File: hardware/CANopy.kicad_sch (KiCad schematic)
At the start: 11 parts, among them J1 RPi_GPIO, J2 CAN0, J3 CAN1, J4 CAN2, U7 AT24C32

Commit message: feat: rename to CANopy
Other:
- sheet CAN0: file can_channel.kicad_sch -> CANopy_branch.kicad_sch
- sheet CAN1: file can_channel.kicad_sch -> CANopy_branch.kicad_sch
- sheet CAN2: file can_channel.kicad_sch -> CANopy_branch.kicad_sch
- title: CAN Hat -> CANopy
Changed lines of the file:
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@@
 	(paper "User" 203.2 127)
 	(title_block
-		(title "CAN Hat")
+		(title "CANopy")
 		(date "2026-04-25")
 		(rev "1")
@@
 		)
 		(instances
-			(project "can-hat"
+			(project "CANopy"
 				(path "/bfdea6a0-b5c8-4489-9fa0-a972c3ff35f2"
 					(reference "J4")
@@
 		)
 		(instances
-			(project "can-hat"
+			(project "CANopy"
 				(path "/bfdea6a0-b5c8-4489-9fa0-a972c3ff35f2"
 					(reference "#PWR040")
@@
 		)
 		(instances
-			(project "can-hat"
+			(project "CANopy"
 				(path "/bfdea6a0-b5c8-4489-9fa0-a972c3ff35f2"
 					(reference "#PWR054")
@@
 		)
 		(instances
-			(project "can-hat"
+			(project "CANopy"
 				(path "/bfdea6a0-b5c8-4489-9fa0-a972c3ff35f2"
 					(reference "C14")
@@
 		)
 		(instances
-			(project "can-hat"
+			(project "CANopy"
 				(path "/bfdea6a0-b5c8-4489-9fa0-a972c3ff35f2"
 					(reference "#PWR041")
@@
 		)
 		(instances
-			(project "can-hat"
+			(project "CANopy"
 				(path "/bfdea6a0-b5c8-4489-9fa0-a972c3ff35f2"
 					(reference "R9")
@@
 		)
 		(instances
-			(project "can-hat"
+			(project "CANopy"
 				(path "/bfdea6a0-b5c8-4489-9fa0-a972c3ff35f2"
 					(reference "#PWR028")
@@
 		)
 		(instances
-			(project "can-hat"
+			(project "CANopy"
 				(path "/bfdea6a0-b5c8-4489-9fa0-a972c3ff35f2"
 					(reference "#PWR030")
@@
 		)
 		(instances
-			(project "can-hat"
+			(project "CANopy"
 				(path "/bfdea6a0-b5c8-4489-9fa0-a972c3ff35f2"
 					(reference "#PWR043")
@@
 		)
 		(instances
-			(project "can-hat"
+			(project "CANopy"
 				(path "/bfdea6a0-b5c8-4489-9fa0-a972c3ff35f2"
 					(reference "#PWR042")
@@
 		)
 		(instances
-			(project "can-hat"
+			(project "CANopy"
 				(path "/bfdea6a0-b5c8-4489-9fa0-a972c3ff35f2"
 					(reference "#PWR052")
@@
 		)
 		(instances
-			(project "can-hat"
+			(project "CANopy"
 				(path "/bfdea6a0-b5c8-4489-9fa0-a972c3ff35f2"
 					(reference "#PWR018")
@@
 		)
 		(instances
-			(project "can-hat"
+			(project "CANopy"
 				(path "/bfdea6a0-b5c8-4489-9fa0-a972c3ff35f2"
 					(reference "#PWR046")
@@
 		)
 		(instances
-			(project "can-hat"
+			(project "CANopy"
 				(path "/bfdea6a0-b5c8-4489-9fa0-a972c3ff35f2"
 					(reference "R8")
@@
 		)
 		(instances
-			(project "can-hat"
+			(project "CANopy"
 				(path "/bfdea6a0-b5c8-4489-9fa0-a972c3ff35f2"
 					(reference "#PWR047")
@@
 		)
 		(instances
-			(project "can-hat"
+			(project "CANopy"
 				(path "/bfdea6a0-b5c8-4489-9fa0-a972c3ff35f2"
 					(reference "#PWR049")
@@
 		)
 		(instances
-			(project "can-hat"
+			(project "CANopy"
 				(path "/bfdea6a0-b5c8-4489-9fa0-a972c3ff35f2"
 					(reference "#PWR050")
@@
 		)
 		(instances
-			(project "can-hat"
+			(project "CANopy"
 				(path "/bfdea6a0-b5c8-4489-9fa0-a972c3ff35f2"
 					(reference "#FLG02")
@@
 		)
 		(instances
-			(project "can-hat"
+			(project "CANopy"
 				(path "/bfdea6a0-b5c8-4489-9fa0-a972c3ff35f2"
 					(reference "J3")
@@
 		)
 		(instances
-			(project "can-hat"
+			(project "CANopy"
 				(path "/bfdea6a0-b5c8-4489-9fa0-a972c3ff35f2"
 					(reference "#PWR045")
@@
 		)
 		(instances
-			(project "can-hat"
+			(project "CANopy"
 				(path "/bfdea6a0-b5c8-4489-9fa0-a972c3ff35f2"
 					(reference "#PWR053")
@@
 		)
 		(instances
-			(project "can-hat"
+			(project "CANopy"
 				(path "/bfdea6a0-b5c8-4489-9fa0-a972c3ff35f2"
 					(reference "#PWR051")
@@
 		)
 		(instances
-			(project "can-hat"
+			(project "CANopy"
 				(path "/bfdea6a0-b5c8-4489-9fa0-a972c3ff35f2"
 					(reference "#FLG03")
@@
 		)
 		(instances
-			(project "can-hat"
+			(project "CANopy"
 				(path "/bfdea6a0-b5c8-4489-9fa0-a972c3ff35f2"
 					(reference "#PWR055")
@@
 		)
 		(instances
-			(project "can-hat"
+			(project "CANopy"
 				(path "/bfdea6a0-b5c8-4489-9fa0-a972c3ff35f2"
 					(reference "#PWR048")
@@
 		)
 		(instances
-			(project "can-hat"
+			(project "CANopy"
 				(path "/bfdea6a0-b5c8-4489-9fa0-a972c3ff35f2"
 					(reference "#PWR016")
@@
 		)
 		(instances
-			(project "can-hat"
+			(project "CANopy"
 				(path "/bfdea6a0-b5c8-4489-9fa0-a972c3ff35f2"
 					(reference "#PWR044")
@@
 			)
 		)
-		(property "Sheetfile" "can_channel.kicad_sch"
+		(property "Sheetfile" "CANopy_branch.kicad_sch"
 			(at 17.526 75.438 90)
 			(effects
@@
 		)
 		(instances
-			(project "can-hat"
+			(project "CANopy"
 				(path "/bfdea6a0-b5c8-4489-9fa0-a972c3ff35f2"
 					(page "3")
@@
 			)
 		)
-		(property "Sheetfile" "can_channel.kicad_sch"
+		(property "Sheetfile" "CANopy_branch.kicad_sch"
 			(at 17.526 107.188 90)
 			(effects
@@
 		)
 		(instances
-			(project "can-hat"
+			(project "CANopy"
 				(path "/bfdea6a0-b5c8-4489-9fa0-a972c3ff35f2"
 					(page "4")
@@
 			)
 		)
-		(property "Sheetfile" "can_channel.kicad_sch"
+		(property "Sheetfile" "CANopy_branch.kicad_sch"
 			(at 17.526 43.688 90)
 			(effects
@@
 		)
 		(instances
-			(project "can-hat"
+			(project "CANopy"
 				(path "/bfdea6a0-b5c8-4489-9fa0-a972c3ff35f2"
 					(page "2")

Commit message: feat: update schematic with proper cap sizes
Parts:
- R7, R8, R9: footprint Resistor_SMD:R_0201_0603Metric -> Resistor_SMD:R_0603_1608Metric
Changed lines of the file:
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@@
 			)
 		)
-		(property "Footprint" "Resistor_SMD:R_0201_0603Metric"
+		(property "Footprint" "Resistor_SMD:R_0603_1608Metric"
 			(at 90.17 63.5 0)
 			(effects
@@
 			)
 		)
-		(property "Footprint" "Resistor_SMD:R_0201_0603Metric"
+		(property "Footprint" "Resistor_SMD:R_0603_1608Metric"
 			(at 91.44 27.94 0)
 			(effects
@@
 			)
 		)
-		(property "Footprint" "Resistor_SMD:R_0201_0603Metric"
+		(property "Footprint" "Resistor_SMD:R_0603_1608Metric"
 			(at 81.28 27.94 0)
 			(effects

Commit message: feat: first pass reroute
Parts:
- added TP5: SDA SCL, symbol Connector:TestPoint_Alt
- J2, J3, J4: footprint Degson:SHDRRA2W80P0X350_1X2_780X920X722P -> Degson:CONN-TH_DG500-5.08-02P-14-00A-H
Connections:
- net CAN0/CAN_N: now also J2.1 (Pin_1); no longer J2.2 (Pin_2)
- net CAN0/CAN_P: now also J2.2 (Pin_2); no longer J2.1 (Pin_1)
- net CAN1/CAN_N: now also J3.1 (Pin_1); no longer J3.2 (Pin_2)
- net CAN1/CAN_P: now also J3.2 (Pin_2); no longer J3.1 (Pin_1)
- net CAN2/CAN_N: now also J4.1 (Pin_1); no longer J4.2 (Pin_2)
- net CAN2/CAN_P: now also J4.2 (Pin_2); no longer J4.1 (Pin_1)
- net ID_SC: now also TP5.1 (TX)
- net ID_SD: now also TP5.1 (TX)
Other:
- note added: "0.2032"
- moved on the sheet: C13, C14, J1, J2, J3, J4, R7, R8, R9, TP1, U7

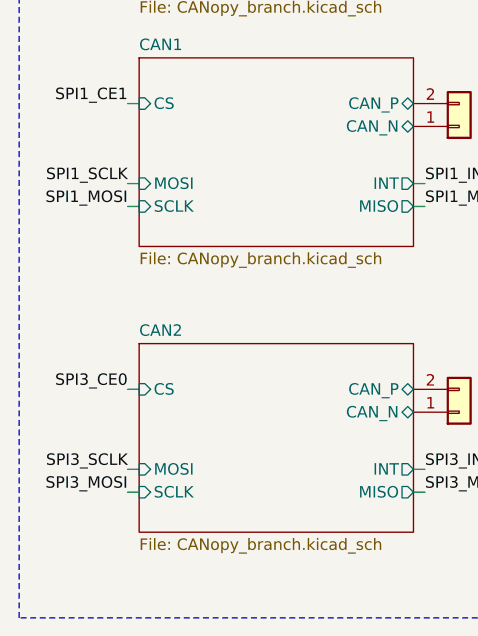
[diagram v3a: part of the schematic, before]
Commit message: feat: route 4 layer
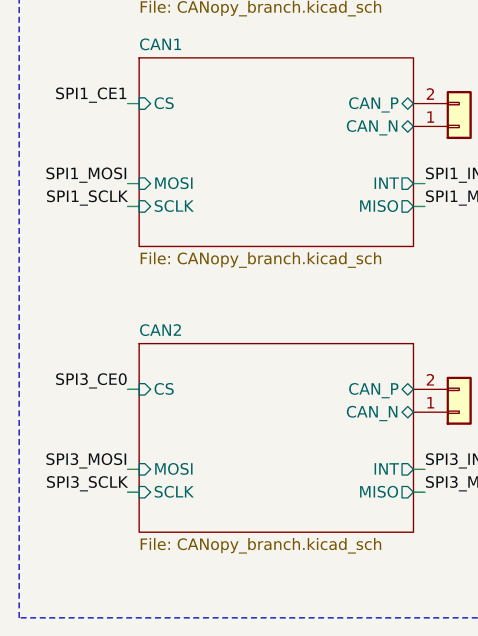
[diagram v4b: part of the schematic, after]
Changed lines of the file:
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@@
+		)
+	)
+	(label "SPI3_MOSI"
+		(at 26.67 96.52 180)
+		(effects
+			(font
+				(size 1.27 1.27)
+			)
+			(justify right bottom)
+		)
+	)
+	(label "SPI1_MOSI"
+		(at 26.67 64.77 180)
+		(effects
+			(font
+				(size 1.27 1.27)
+			)
+			(justify right bottom)
 		)
 	)
@@
 		)
 	)
+	(label "SPI1_SCLK"
+		(at 26.67 39.37 180)
+		(effects
+			(font
+				(size 1.27 1.27)
+			)
+			(justify right bottom)
+		)
+	)
 	(label "SPI1_INT0"
 		(at 198.12 41.91 0)
@@
 		)
 	)
-	(label "SPI3_MOSI"
-		(at 26.67 99.06 180)
-		(effects
-			(font
-				(size 1.27 1.27)
-			)
-			(justify right bottom)
-		)
-	)
 	(label "SPI1_MISO"
 		(at 59.69 67.31 0)
@@
 	)
 	(label "SPI1_SCLK"
-		(at 26.67 64.77 180)
+		(at 26.67 67.31 180)
 		(effects
 			(font
@@
 		)
 	)
+	(label "SPI1_MOSI"
+		(at 26.67 36.83 180)
+		(effects
+			(font
+				(size 1.27 1.27)
+			)
+			(justify right bottom)
+		)
+	)
+	(label "SPI3_SCLK"
+		(at 26.67 99.06 180)
+		(effects
+			(font
+				(size 1.27 1.27)
+			)
+			(justify right bottom)
+		)
+	)
 	(label "SPI3_MISO"
 		(at 198.12 54.61 0)
@@
 		)
 	)
-	(label "SPI3_SCLK"
-		(at 26.67 96.52 180)
-		(effects
-			(font
-				(size 1.27 1.27)
-			)
-			(justify right bottom)
-		)
-	)
 	(label "ID_SC"
 		(at 198.12 57.15 0)
@@
 		)
 	)
-	(label "SPI1_MOSI"
-		(at 26.67 67.31 180)
-		(effects
-			(font
-				(size 1.27 1.27)
-			)
-			(justify right bottom)
-		)
-	)
 	(label "WriteProtect"
 		(at 110.49 59.69 0)
@@
 		)
 	)
-	(label "SPI1_SCLK"
-		(at 26.67 39.37 180)
-		(effects
-			(font
-				(size 1.27 1.27)
-			)
-			(justify right bottom)
-		)
-	)
-	(label "SPI1_MOSI"
-		(at 26.67 36.83 180)
-		(effects
-			(font
-				(size 1.27 1.27)
-			)
-			(justify right bottom)
-		)
-	)
